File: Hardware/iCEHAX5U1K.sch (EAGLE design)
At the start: 28 parts, among them IC1 ICE5LP1K-SG48, IC2 XC6206P331MR-G, IC3 XC6206P122MR-G, IC4 STM32F042F6P6, IC5 BR24G1MFJ-3AGTE2

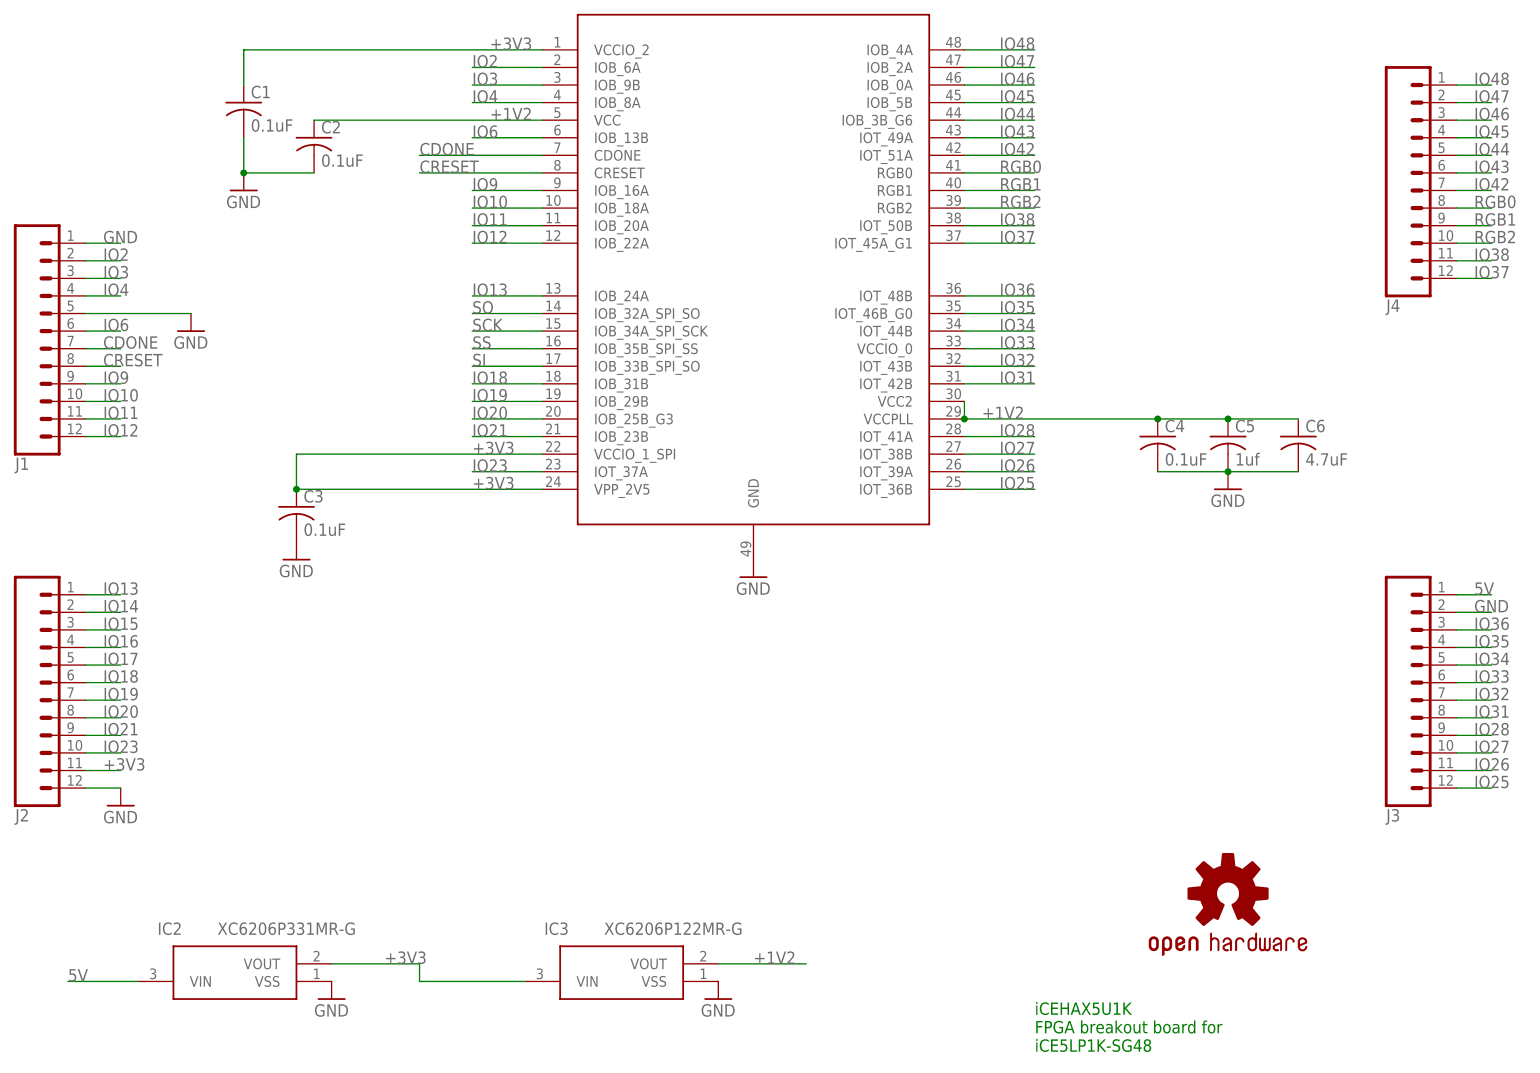
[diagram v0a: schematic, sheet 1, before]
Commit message: Top PIO Bank design issue fixed. - Top PIO Bank (Pin 25 and up) was missing the VCC_IO rail due to confusion of pin 33.
Signed-off-by: Tin LetHax <thipok17@gmail.com>
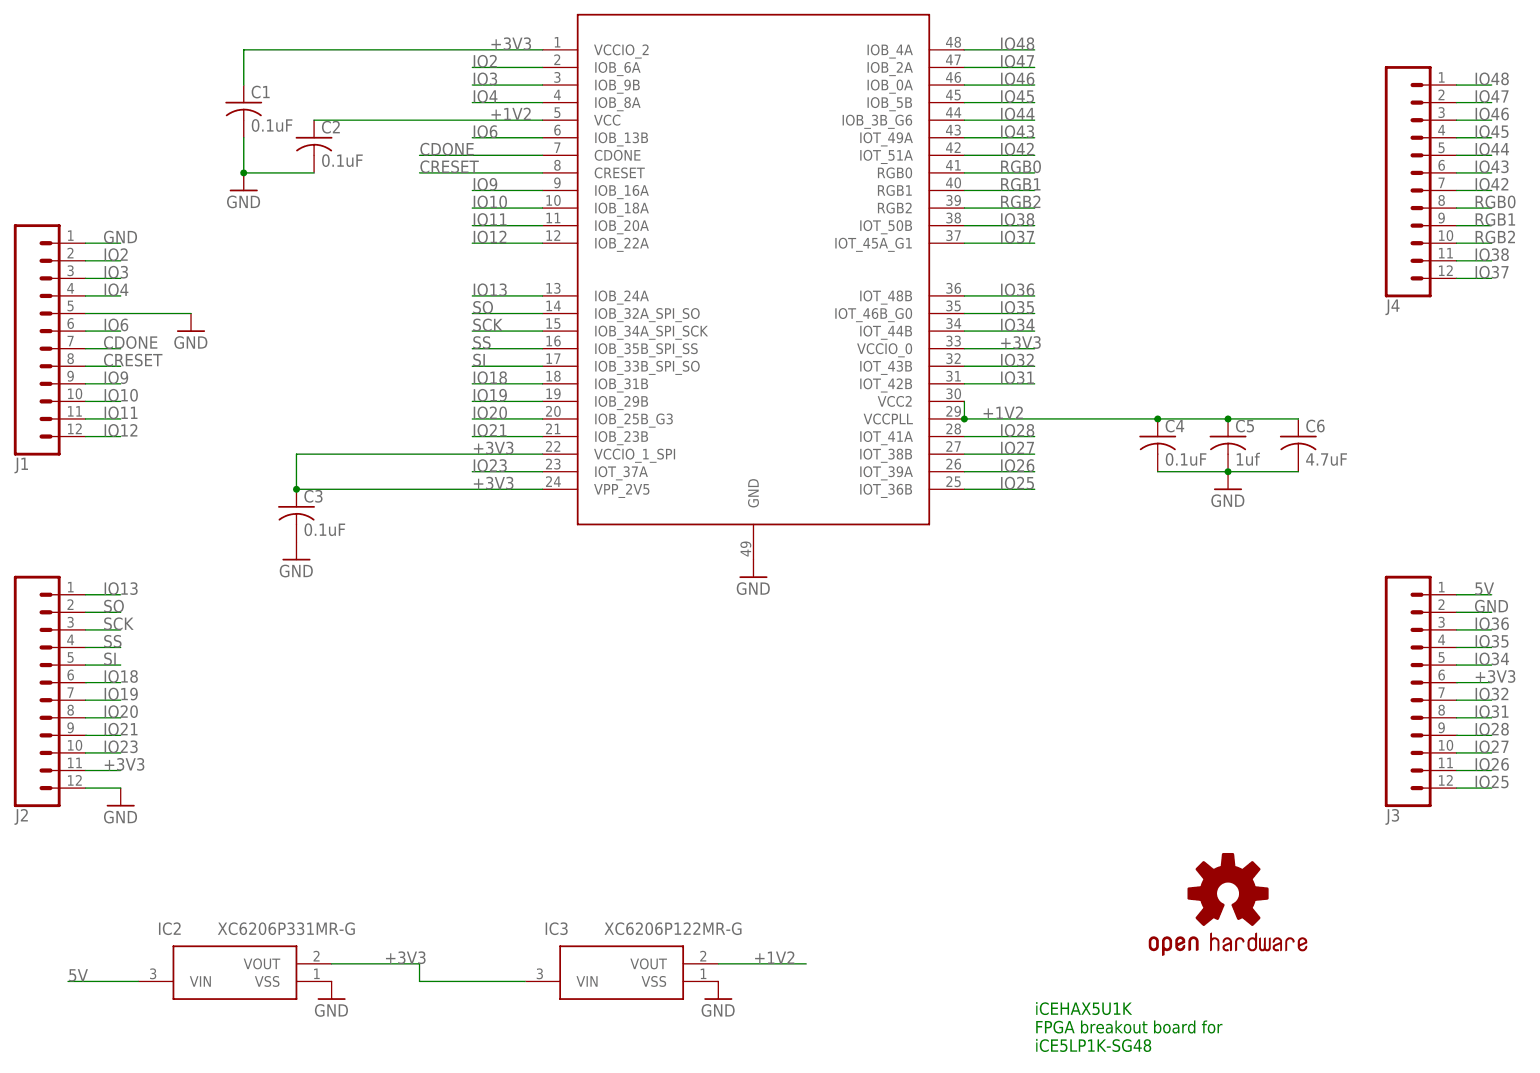
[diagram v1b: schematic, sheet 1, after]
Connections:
- removed net IO14: J2.2
- removed net IO15: J2.3
- removed net IO16: J2.4
- removed net IO17: J2.5
- removed net IO33: IC1.VCCIO_0, J3.6
- net +3V3: now also IC1.VCCIO_0, J3.6
- net SCK: now also J2.3
- net SI: now also J2.5
- net SO: now also J2.2
- net SS: now also J2.4
